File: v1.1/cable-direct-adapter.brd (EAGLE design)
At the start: 19 parts, among them J2 SSM-120-L-DV

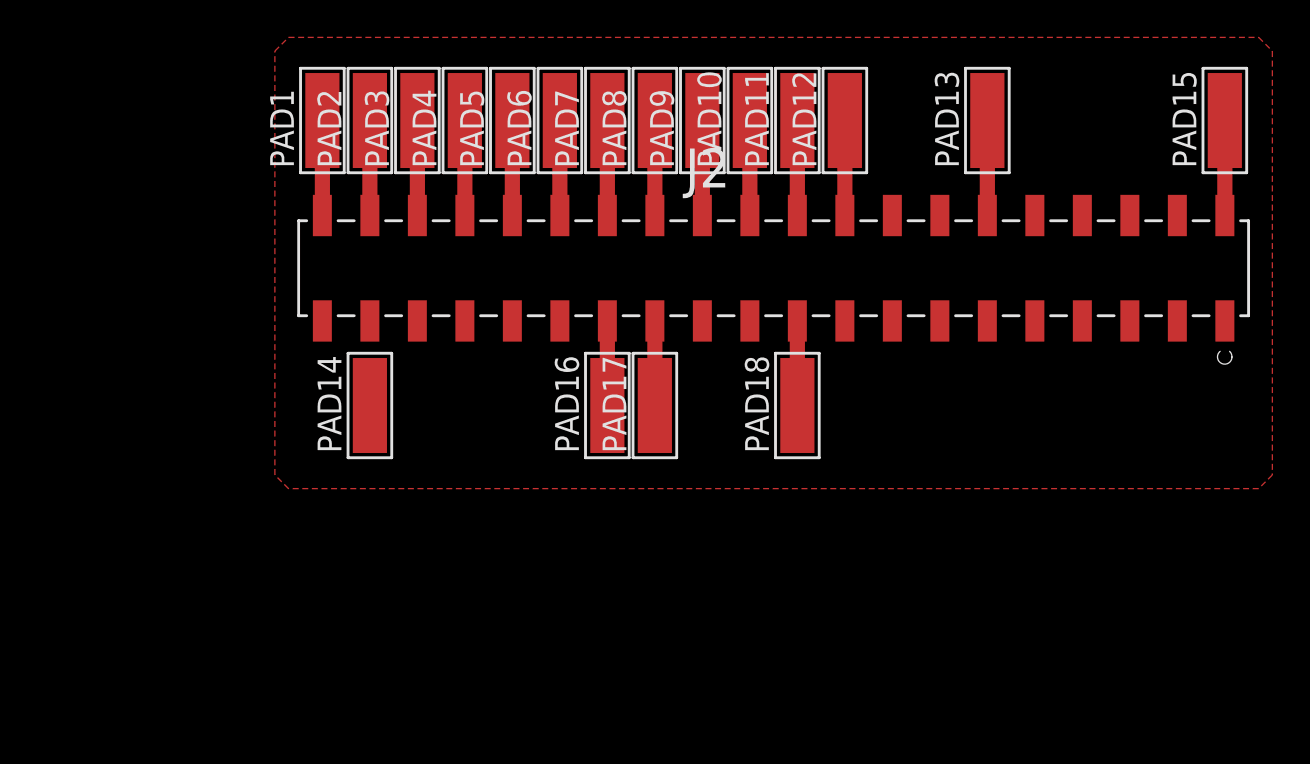
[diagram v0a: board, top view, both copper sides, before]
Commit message: add xilinx code and finish direct adapter
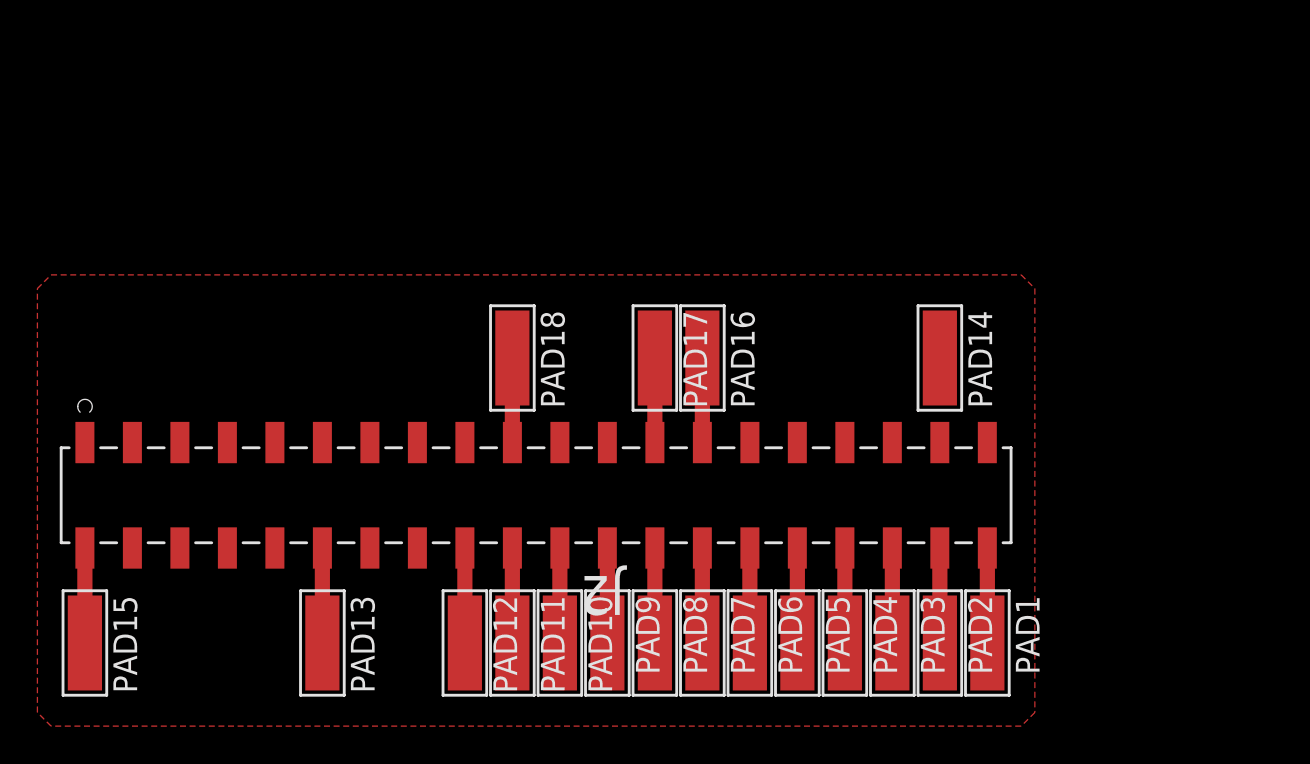
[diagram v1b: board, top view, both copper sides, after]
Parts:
- moved PAD15 67.1 mm to (3.81, 6.35), turned to 180 degrees
- moved PAD1 45.2 mm to (52.1, 6.35), turned to 180 degrees
- moved PAD13 45.2 mm to (16.5, 6.35), turned to 180 degrees
- moved PAD2 41.3 mm to (49.5, 6.35), turned to 180 degrees
- moved J2 39.8 mm to (52.1, 11.4), turned to 180 degrees
- moved PAD3 37.8 mm to (47.0, 6.35), turned to 180 degrees
- moved PAD12 34.5 mm to (24.1, 6.35), turned to 180 degrees
- moved PAD4 34.5 mm to (44.5, 6.35), turned to 180 degrees
- moved PAD11 31.8 mm to (26.7, 6.35), turned to 180 degrees
- moved PAD5 31.8 mm to (41.9, 6.35), turned to 180 degrees
- moved PAD14 30.6 mm to (49.5, 21.6), turned to 180 degrees
- moved PAD10 29.7 mm to (29.2, 6.35), turned to 180 degrees
- moved PAD6 29.7 mm to (39.4, 6.35), turned to 180 degrees
- moved PAD7 28.4 mm to (36.8, 6.35), turned to 180 degrees
- moved PAD9 28.4 mm to (31.8, 6.35), turned to 180 degrees
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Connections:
- removed net N$1: J2.1
- removed net N$10: J2.17
- removed net N$11: J2.21
- removed net N$12: J2.23
- removed net N$13: J2.33
- removed net N$14: J2.39
- removed net N$2: J2.3
- removed net N$3: J2.5
- removed net N$5: J2.7
- removed net N$6: J2.9
- removed net N$7: J2.11
- removed net N$8: J2.13
- removed net N$9: J2.15
